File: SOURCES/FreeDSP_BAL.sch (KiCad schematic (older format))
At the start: 187 parts, among them IC1 AD8608ARZ, IC2 ADAU1701, IC3 24AA256, IC4 SN74LVC1G08DBVR, IC5 AD8608ARZ, IC6 AD8608ARZ, IC7 74HC4040D, P10 CONN_02X10, P11 MM-16G, P12 MM-12G, P2 BARREL_JACK, P3 CONN_02X02, P4 USBi, P5 CONN_02X13, P6 CONN_01X06, P7 CONN_01X06, P8 CONN_01X06, P9 CONN_02X10, Q1 ZXTP25040DFHTA, Q2 2N7000, Q3 2N7000, U1 78033, U3 7805

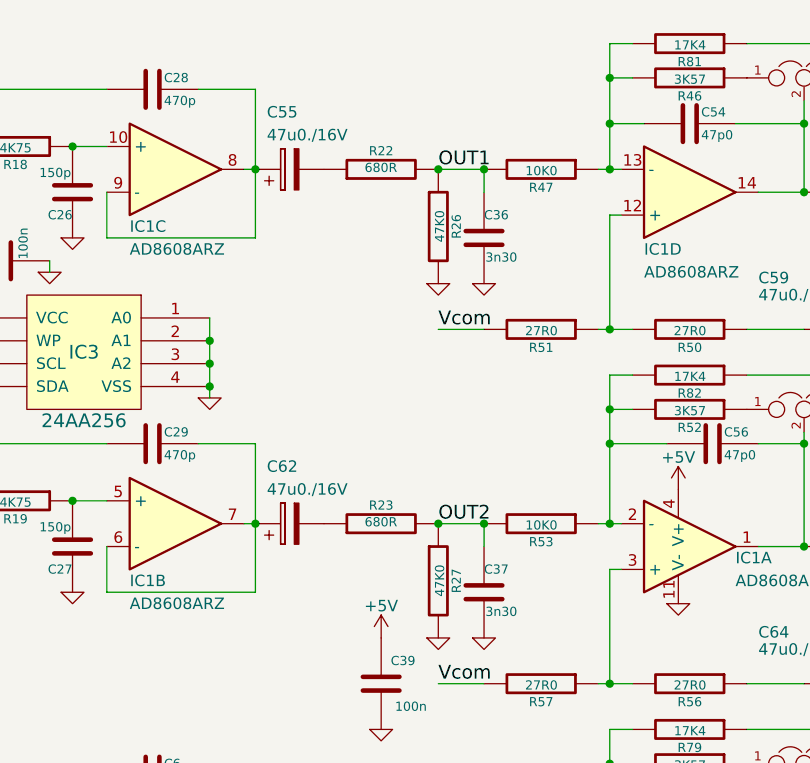
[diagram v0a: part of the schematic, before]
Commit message: Correction of some typos
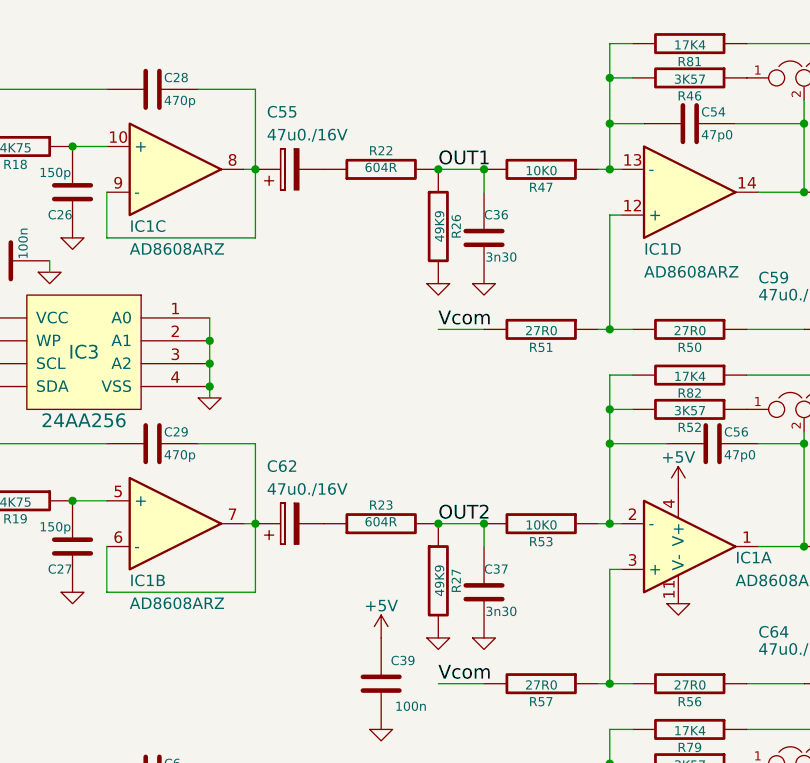
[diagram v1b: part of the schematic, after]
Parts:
- R22, R23: value 680R -> 604R
- R26, R27: value 47K0 -> 49K9
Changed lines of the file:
@@
 P 8450 2950
 F 0 "R27" V 8530 2950 40  0000 C CNN
-F 1 "47K0" V 8457 2951 40  0000 C CNN
+F 1 "49K9" V 8457 2951 40  0000 C CNN
 F 2 "rklib:C0805-RES" V 8380 2950 30  0001 C CNN
 F 3 "~" H 8450 2950 30  0000 C CNN
@@
 P 8200 2700
 F 0 "R23" V 8280 2700 40  0000 C CNN
-F 1 "680R" V 8207 2701 40  0000 C CNN
+F 1 "604R" V 8207 2701 40  0000 C CNN
 F 2 "rklib:C0805-RES" V 8130 2700 30  0001 C CNN
 F 3 "~" H 8200 2700 30  0000 C CNN
@@
 P 8450 1400
 F 0 "R26" V 8530 1400 40  0000 C CNN
-F 1 "47K0" V 8457 1401 40  0000 C CNN
+F 1 "49K9" V 8457 1401 40  0000 C CNN
 F 2 "rklib:C0805-RES" V 8380 1400 30  0001 C CNN
 F 3 "~" H 8450 1400 30  0000 C CNN
@@
 P 8200 1150
 F 0 "R22" V 8280 1150 40  0000 C CNN
-F 1 "680R" V 8207 1151 40  0000 C CNN
+F 1 "604R" V 8207 1151 40  0000 C CNN
 F 2 "rklib:C0805-RES" V 8130 1150 30  0001 C CNN
 F 3 "~" H 8200 1150 30  0000 C CNN

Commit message: Chaged OSC1 to 24.576MHz
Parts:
- OSC1: value 12M288Hz -> 24M576Hz
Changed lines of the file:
@@
 U 1 1 55397564
 P 4200 3000
-F 0 "OSC1" H 4200 3150 60  0000 C CNN
-F 1 "12M288Hz" H 4200 2850 60  0000 C CNN
+F 0 "OSC1" H 4050 3250 60  0000 C CNN
+F 1 "24M576Hz" H 4150 3150 60  0000 C CNN
 F 2 "Crystals:Crystal_HC49-SD_SMD" H 4200 3000 60  0001 C CNN
 F 3 "~" H 4200 3000 60  0000 C CNN

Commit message: Changed voltage divider for outputs to avoid clipping for full scale (ADAU1701 on prototype gives 2.8Vpp instead of 2.5Vpp)
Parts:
- R22, R23, R7, R8: value 604R -> 6K04
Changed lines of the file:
@@
 P 8200 4150
 F 0 "R8" V 8280 4150 40  0000 C CNN
-F 1 "604R" V 8207 4151 40  0000 C CNN
+F 1 "6K04" V 8207 4151 40  0000 C CNN
 F 2 "rklib:C0805-RES" V 8130 4150 30  0001 C CNN
 F 3 "~" H 8200 4150 30  0000 C CNN
@@
 P 8200 5700
 F 0 "R7" V 8280 5700 40  0000 C CNN
-F 1 "604R" V 8207 5701 40  0000 C CNN
+F 1 "6K04" V 8207 5701 40  0000 C CNN
 F 2 "rklib:C0805-RES" V 8130 5700 30  0001 C CNN
 F 3 "~" H 8200 5700 30  0000 C CNN
@@
 P 8200 2700
 F 0 "R23" V 8280 2700 40  0000 C CNN
-F 1 "604R" V 8207 2701 40  0000 C CNN
+F 1 "6K04" V 8207 2701 40  0000 C CNN
 F 2 "rklib:C0805-RES" V 8130 2700 30  0001 C CNN
 F 3 "~" H 8200 2700 30  0000 C CNN
@@
 P 8200 1150
 F 0 "R22" V 8280 1150 40  0000 C CNN
-F 1 "604R" V 8207 1151 40  0000 C CNN
+F 1 "6K04" V 8207 1151 40  0000 C CNN
 F 2 "rklib:C0805-RES" V 8130 1150 30  0001 C CNN
 F 3 "~" H 8200 1150 30  0000 C CNN

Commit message: Changed expansion header to 2.54 IDC
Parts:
- P11: value MM-16G -> IDC-16G; footprint rklib:MM-16G -> Connect:IDC_Header_Straight_16pins
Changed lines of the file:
@@
 P 550 4800
 F 0 "P11" H 550 5650 50  0000 C CNN
-F 1 "MM-16G" H 450 3900 50  0000 C CNN
-F 2 "rklib:MM-16G" H 550 4800 50  0001 C CNN
+F 1 "IDC-16G" H 450 3900 50  0000 C CNN
+F 2 "Connect:IDC_Header_Straight_16pins" H 550 4800 50  0001 C CNN
 F 3 "" H 550 4800 50  0000 C CNN
 	1    550  4800

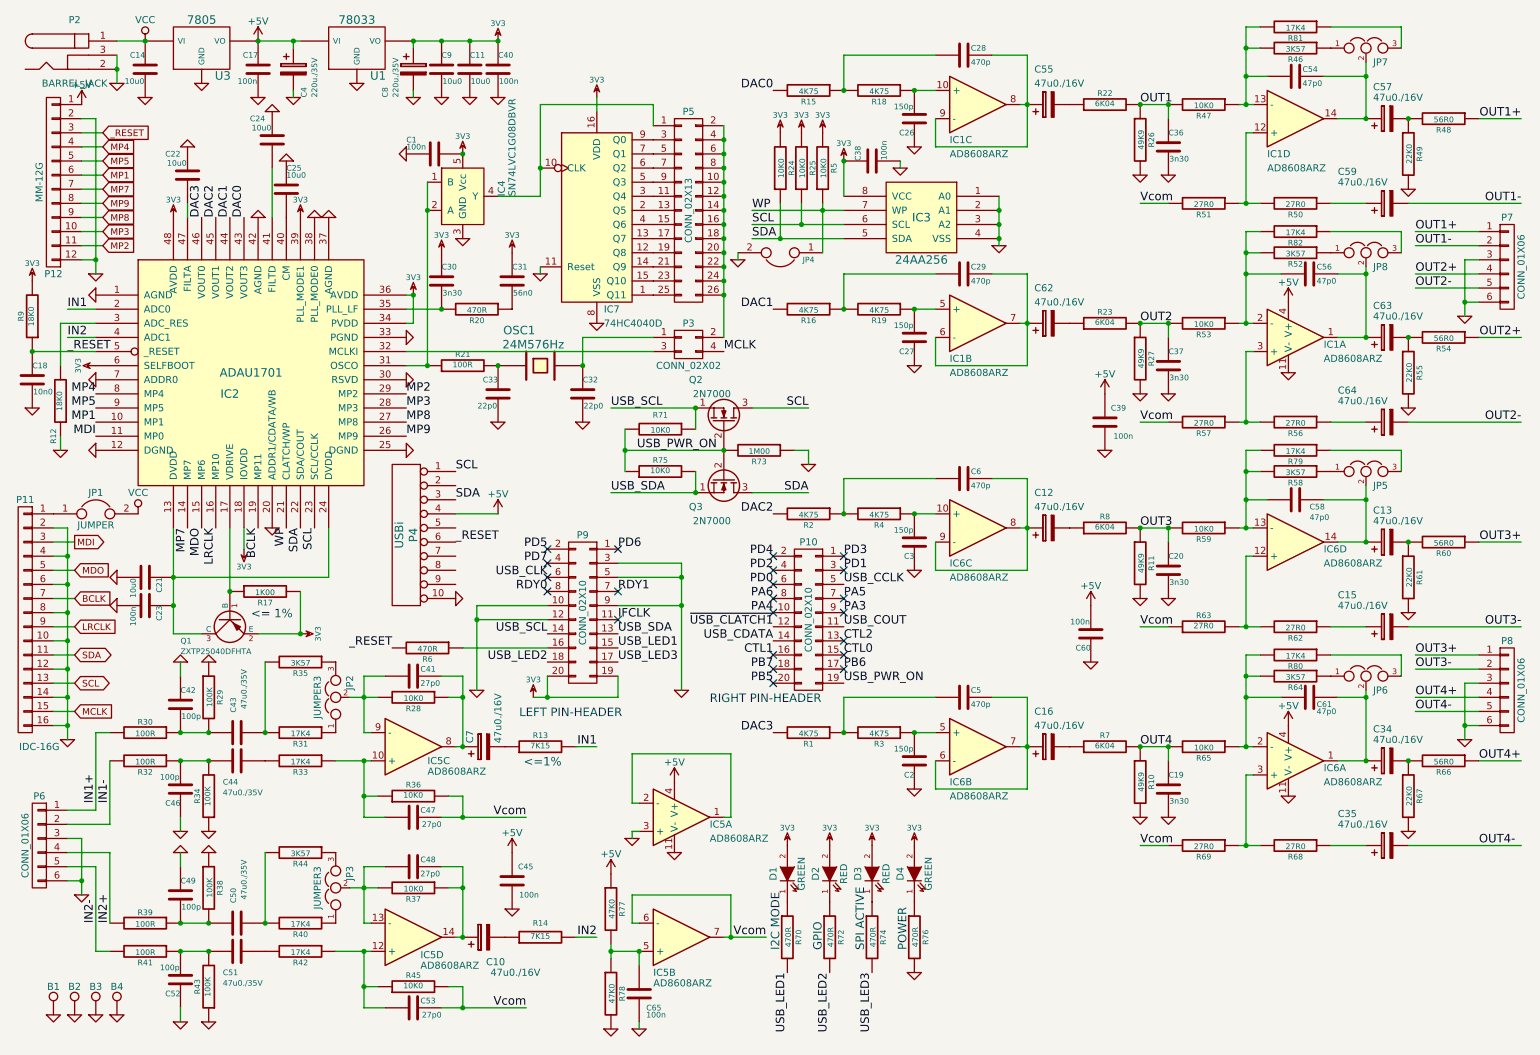
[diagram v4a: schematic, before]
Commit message: Revision C: Improvement of input and output stages. Added some fault protection.
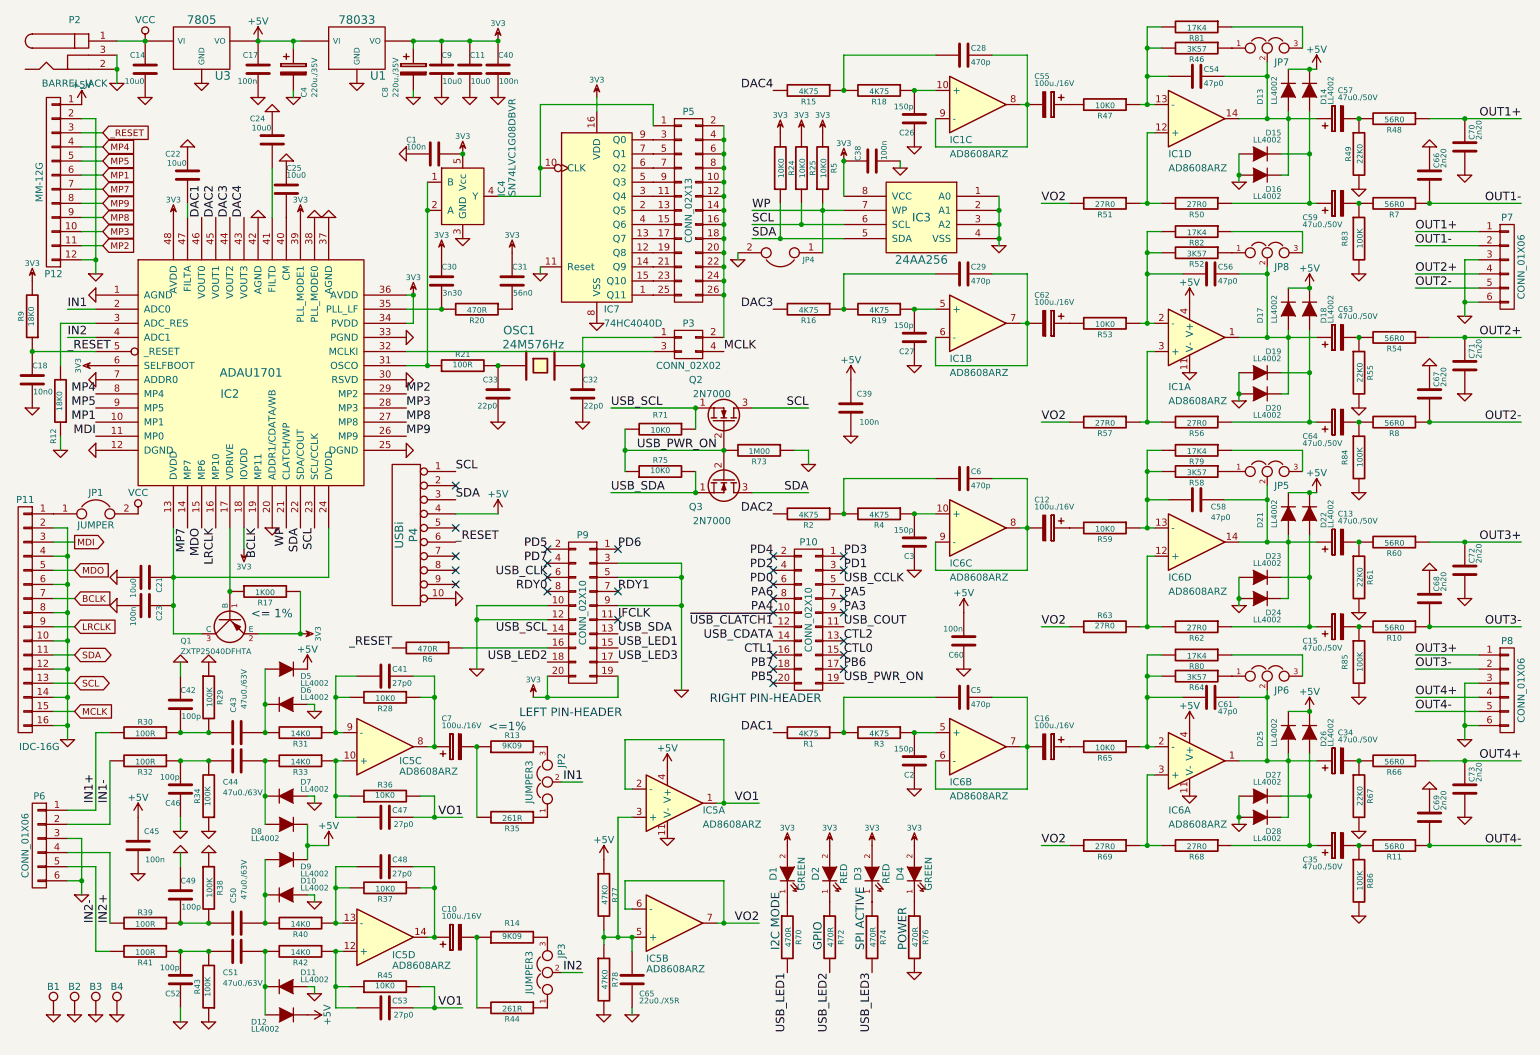
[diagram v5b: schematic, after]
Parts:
- removed C19, C20, C36, C37: 3n30, rklib:C0805-X7R, symbol C-RESCUE-FreeDSP_SMD
- removed R22, R23: 6K04, rklib:C0805-RES, symbol R-RESCUE-FreeDSP_SMD
- removed R26, R27: 49K9, rklib:C0805-RES, symbol R-RESCUE-FreeDSP_SMD
- added C66, C67, C68, C69, C70, C71, C72, C73: 2n20, rklib:C0805-X7R, symbol C-RESCUE-FreeDSP_SMD
- added D10, D11, D12, D13, D14, D15, D16, D17, D18, D19, D20, D21, D22, D23, D24, D25, D26, D27, D28, D5, D6, D7, D8, D9: LL4002, Diodes_SMD:MELF_Standard, symbol D
- added R83, R84, R85, R86: 100K, rklib:C0805-RES, symbol R-RESCUE-FreeDSP_SMD
- C10, C12, C16, C55, C62, C7: value 47u0./16V -> 100u./16V
- C13, C15, C34, C35, C57, C59, C63, C64: value 47u0./16V -> 47u0./50V; footprint Capacitors_ThroughHole:C_Radial_D5_L11_P2 -> Capacitors_ThroughHole:C_Radial_D6.3_L11.2_P2.5
- C43, C44, C50, C51: value 47u0./35V -> 47u0./63V; footprint Capacitors_ThroughHole:C_Radial_D8_L11.5_P3.5 -> Capacitors_ThroughHole:C_Radial_D10_L16_P5
- C65: value 100n -> 22u0./X5R
- R10, R11: value 49K9 -> 56R0
- R13, R14: value 7K15 -> 9K09
- R31, R33, R40, R42: value 17K4 -> 14K0
- R35, R44: value 3K57 -> 261R
- R7, R8: value 6K04 -> 56R0
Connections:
- net +5V: now also D12.1 (K), D13.1 (K), D14.1 (K), D17.1 (K), D18.1 (K), D21.1 (K), D22.1 (K), D25.1 (K), D26.1 (K), D5.1 (K), D8.1 (K), D9.1 (K)
- net DAC1: now also IC2.46 (VOUT0), R1.2; no longer IC2.44 (VOUT2), R16.2
- net DAC3: now also IC2.44 (VOUT2), R16.2; no longer IC2.46 (VOUT0), R1.2
- net GND: now also C66.2, C67.2, C68.2, C69.2, C70.1, C71.1, C72.1, C73.1, D10.2 (A), D11.2 (A), D15.2 (A), D16.2 (A), D19.2 (A), D20.2 (A), D23.2 (A), D24.2 (A), D27.2 (A), D28.2 (A), D6.2 (A), D7.2 (A), R83.2, R84.2, R85.2, R86.2; no longer IC5.3 (+), R10.2, R11.2
- net IN1: now also JP2.2; no longer R13.2
- net IN2: now also JP3.2; no longer R14.2
- net OUT1+: now also C70.2
- net OUT1-: now also R7.1, C66.1; no longer C59.2
- net OUT2+: now also C71.2
- net OUT2-: now also R8.1, C67.1; no longer C64.2
- net OUT3+: now also C72.2
- net OUT3-: now also R10.1, C68.1; no longer C15.2
- net OUT4+: now also C73.2
- net OUT4-: now also R11.1, C69.1; no longer C35.2
- net at C7.2, R13.1: now also R35.2
- net at C10.2, R14.1: now also R44.2
- net at C28.1, IC1.8, IC1.9 (-): now also C55.2; no longer C55.1
- net at C29.1, IC1.6 (-), IC1.7: now also C62.2; no longer C62.1
- net at C5.1, IC6.6 (-), IC6.7: now also C16.2; no longer C16.1
- net at C6.1, IC6.8, IC6.9 (-): now also C12.2; no longer C12.1
- net at C43.1, R31.2: now also D5.2 (A), D6.1 (K); no longer R35.2
- net at C44.1, R33.2: now also D7.1 (K), D8.2 (A)
- net at C41.2, IC5.9 (-), R28.2: now also R31.1; no longer JP2.2
- net at JP2.1: now also R35.1; no longer R31.1
- net at JP2.3: now also R13.2; no longer R35.1
- net at C50.1, R40.2: now also D10.1 (K), D9.2 (A); no longer R44.2
- net at C51.1, R42.2: now also D11.1 (K), D12.2 (A)
- net at C48.2, IC5.13 (-), R37.2: now also R40.1; no longer JP3.2
- net at JP3.1: now also R44.1; no longer R40.1
- net at JP3.3: now also R14.2; no longer R44.1
- net at C54.1, C57.1, IC1.14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: now also D13.2 (A), D16.1 (K)
- net at C59.1, R50.1: now also D14.2 (A), D15.1 (K)
- net at C56.1, C63.1, IC1.1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: now also D17.2 (A), D20.1 (K)
- net at C64.1, R56.1: now also D18.2 (A), D19.1 (K)
- net at C13.1, C58.1, IC6.14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: now also D21.2 (A), D24.1 (K)
- net at C15.1, R62.1: now also D22.2 (A), D23.1 (K)
- net at C34.1, C61.1, IC6.1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: now also D25.2 (A), D28.1 (K)
- net at C35.1, R68.1: now also D26.2 (A), D27.1 (K)
- net VO1: now reaches IC5.1, IC5.2 (-)
- net VO1: now also C47.2, C53.2, R36.2, R45.2
- net at C65.2, IC5.5 (+), R77.2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: now also IC5.3 (+)
- net DAC0 renamed DAC4
- net OUT1: no longer names the net of R47.2
- net OUT1: now also C55.1
- net OUT2: no longer names the net of R53.2
- net OUT2: now also C62.1
- removed net OUT3: R11.1, R59.2, R8.2
- removed net OUT4: R10.1, R65.2, R7.2
- net Vcom renamed VO2
- net VO2: no longer C47.2, C53.2, R36.2, R45.2
- new net: C12.1, R59.2
- new net: C16.1, R65.2
- new net: C35.2, R11.2, R86.1
- new net: C64.2, R8.2, R84.1
- new net: C59.2, R7.2, R83.1
- new net: C15.2, R10.2, R85.1
- no-connect marks 22 -> 27
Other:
- moved on the sheet: C10, C13, C15, C34, C35, C39, C41, C45, C47, C48, C53, C54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
